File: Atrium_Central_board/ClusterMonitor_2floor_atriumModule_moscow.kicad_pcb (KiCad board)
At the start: 2 copper layers, 135.1 x 143.6 mm, 52 parts, among them J1 RJ32_Shielded, J2 Conn_01x07, SW1 SW_SPST, SW2 ADDRESS_SELECT, SW3 SW_SPDT, U1 AMS1117-3.3, U2 STM32F030C8Tx

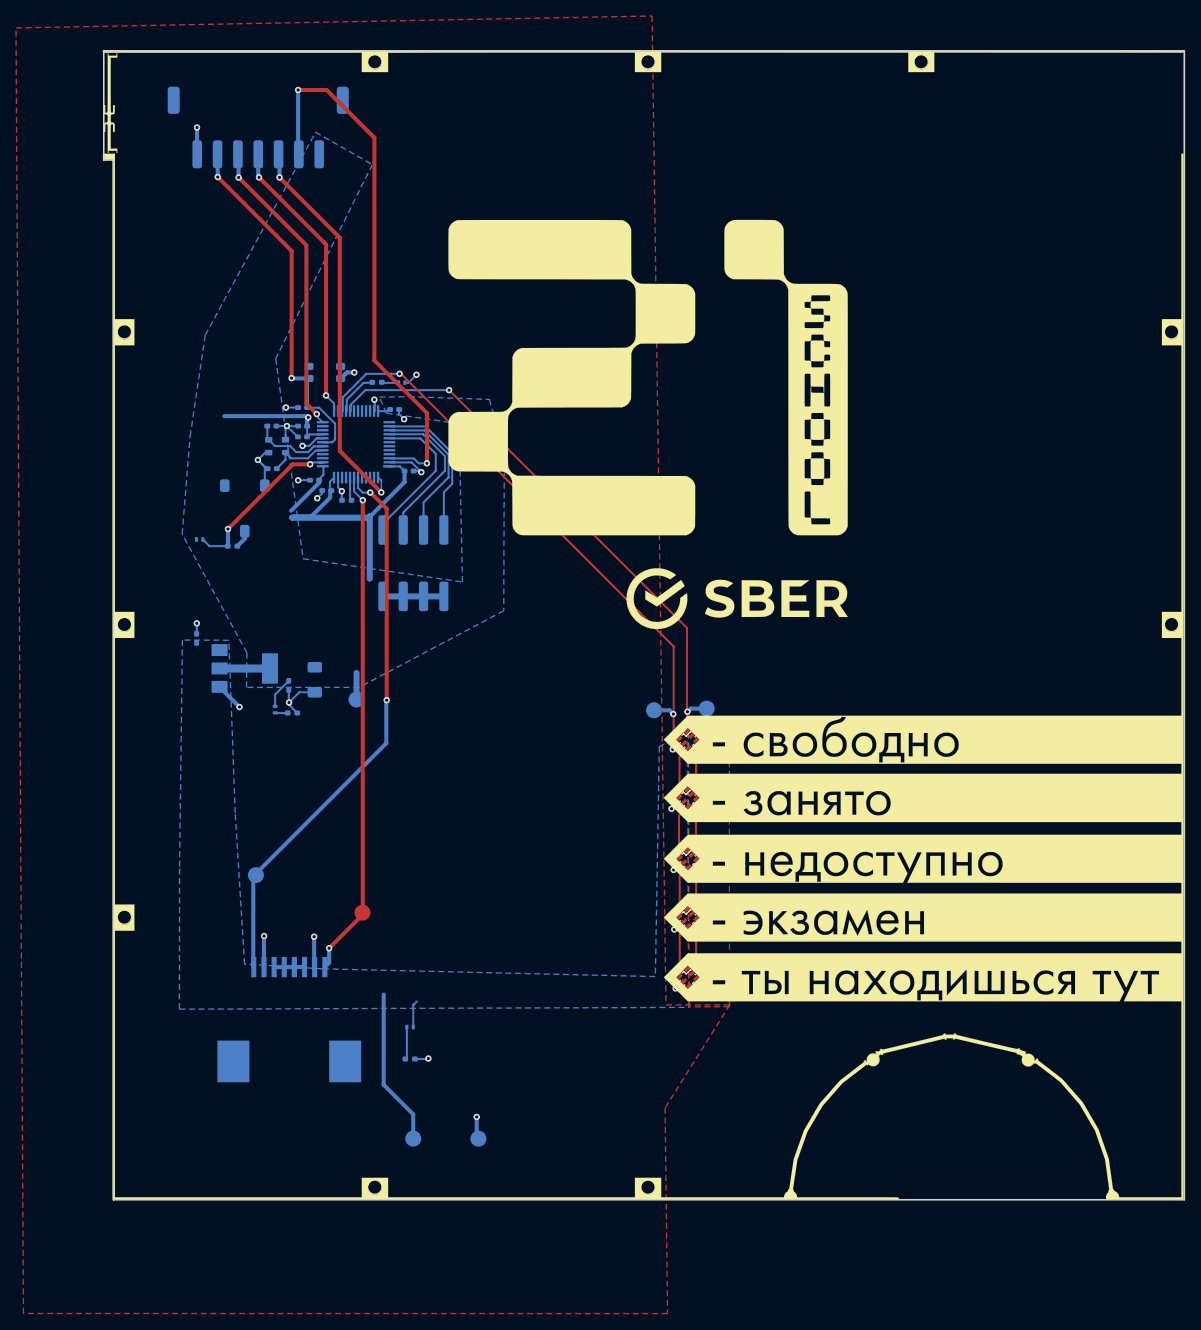
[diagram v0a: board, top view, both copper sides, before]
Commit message: Some changes
Add stencil board layout.
Add gerbers.
Minor changes in expancion and atrium board.
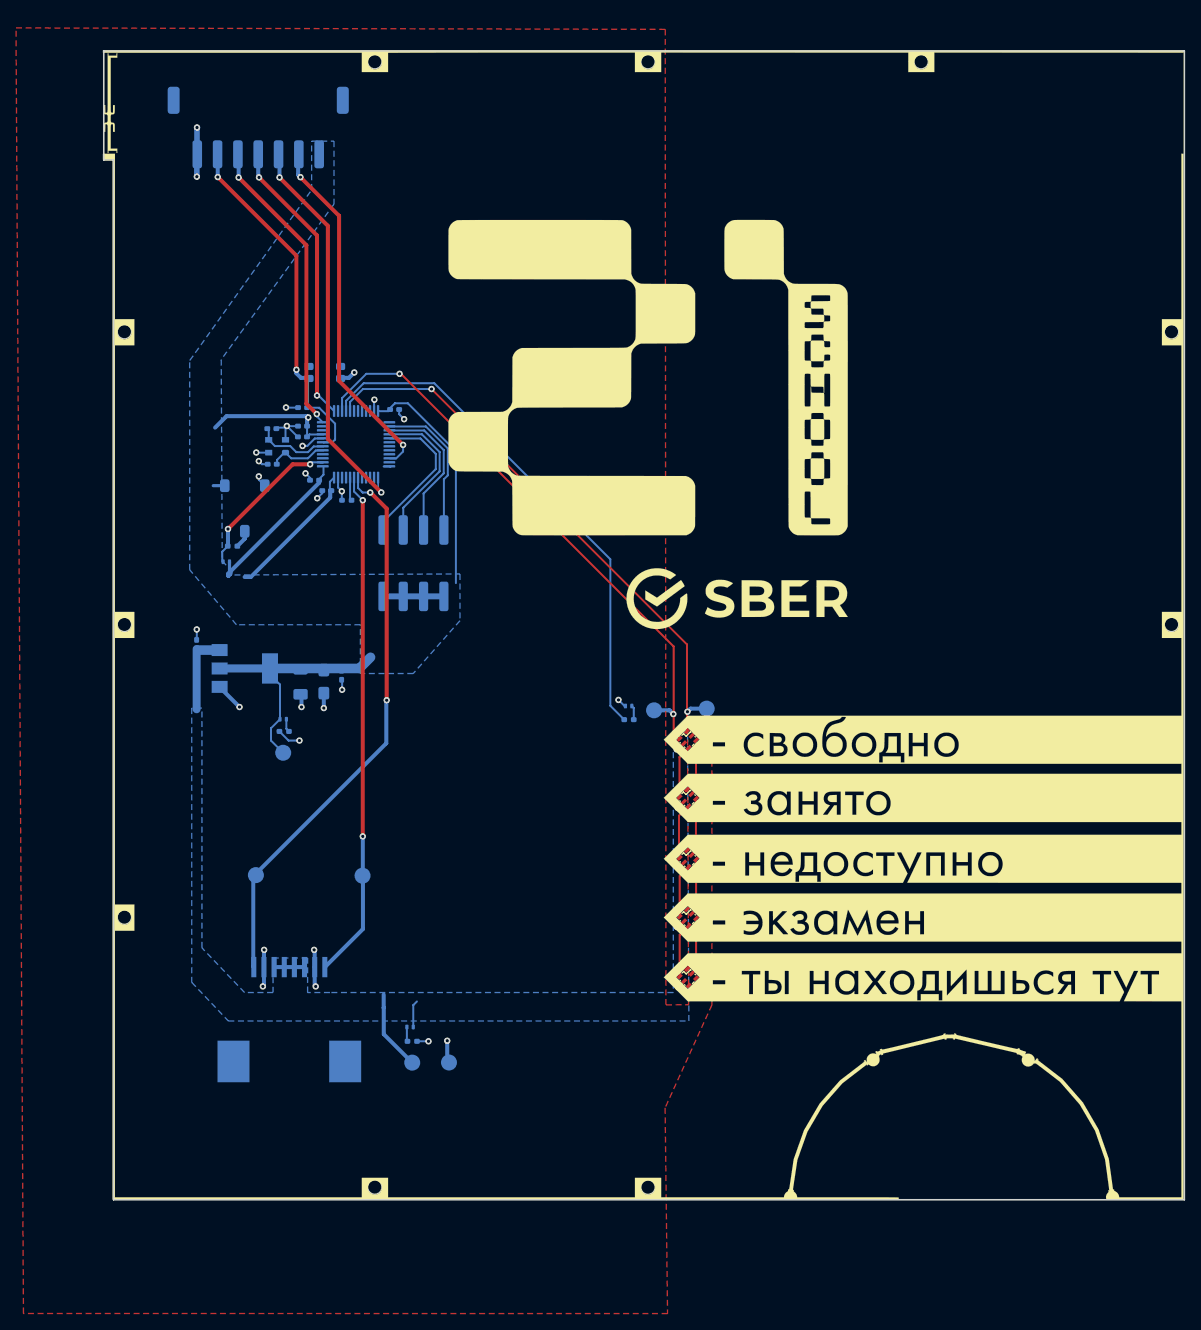
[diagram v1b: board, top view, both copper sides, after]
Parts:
- removed the C9 at (222.2, 58.5)
- added C10: CP_EIA-3216-10_Kemet-I_Pad1.58x1.35mm_HandSolder, Capacitor_Tantalum_SMD:CP_EIA-3216-10_Kemet-I_Pad1.58x1.35mm_HandSolder, B.Cu at (211.6, 84.8)
- added G***: LOGO, ClusterMonitor_silklib:label_atrium_silk_kicad, B.Cu at (264.2, 43.8)
- moved R4 52.6 mm to (249.7, 89.6)
- moved D3 49.4 mm to (249.7, 87.9), turned to 0 degrees
- moved 3v3 11.3 mm to (206.5, 93.7)
- moved GND 10.2 mm to (227.2, 132.4)
- moved 5V 9.50 mm to (222.6, 132.5)
- moved C4 6.73 mm to (213.8, 84.0)
- moved I2C1_SDA 4.63 mm to (216.4, 109.1)
- moved D4 4.34 mm to (199.4, 69.8), turned to 0 degrees
- moved R2 2.52 mm to (206.6, 91.1), turned to 180 degrees
- moved R1 2.23 mm to (222.6, 129.8)
- moved C5 1.80 mm to (208.7, 84.9)
- moved D2 1.57 mm to (206.5, 89.5), turned to 180 degrees
- moved C2 0.76 mm to (195.7, 80.2)
- moved C1 0.55 mm to (205.1, 57.7)
- moved C3 0.32 mm to (205.1, 53.2)
- renumbered VDDA to 3v3, C10 to C9
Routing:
- net Net-(R4-Pad1): track 5.68 -> 65.1 mm
- net VDDA: track 83.3 -> 125.7 mm
- net SYS_JTMS-SWDIO: track 68.4 -> 44.8 mm
- net +5V: track 35.8 -> 33.3 mm
- net Net-(D1-Pad1): track 4.08 -> 1.93 mm
- net REG_4b: track 18.8 -> 17.6 mm
- net SWITCH_MODE: track 21.6 -> 20.6 mm
- net C_RST: track 45.7 -> 44.8 mm
- net Net-(U2-Pad36): track 0.00 -> 0.87 mm
- net SPI1_MOSI: track 71.4 -> 70.6 mm
- net REG_3b: track 19.4 -> 18.8 mm
- net REG_2b: track 19.3 -> 18.8 mm
- net GND: track 63.5 -> 63.2 mm, vias 20 -> 27
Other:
- rule trace_min: 0.2 -> 0.127
- rule via_min_drill: 0.3 -> 0.2
- board text added: "JLCJLCJLCJLC"
- board text added: "RESET"
- board text added: "TEST_MODE"
